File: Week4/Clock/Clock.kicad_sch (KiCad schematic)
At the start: 46 parts, among them J1 Power_inlet_vertical, J2 Conn_01x06, SW1 RotaryEncoder_Switch, SW2 Omron_B3F_SPST, U2 ATmega328-PU, U3 L7805_TO92, U4 DS1307_DIP-8, U5 MAX7219, U6 MAX7219, Y1 Crystal 16MHZ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

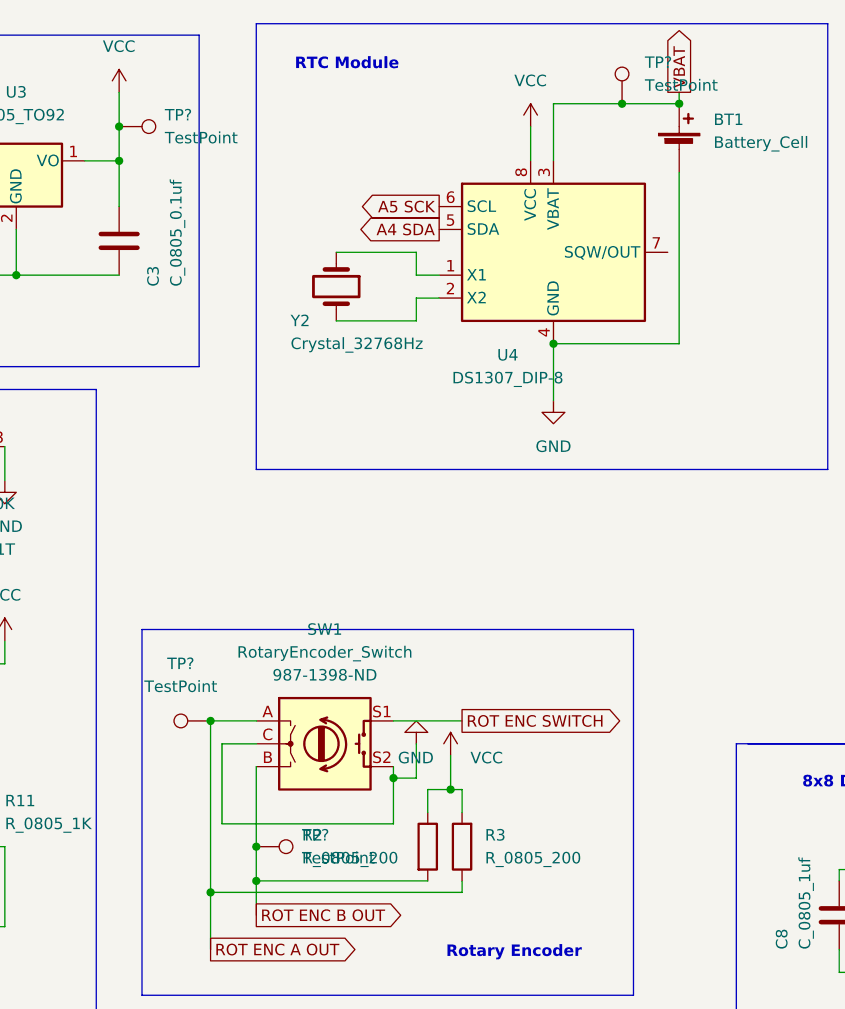
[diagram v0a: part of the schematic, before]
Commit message: Fixed ALL DRC Warnings
Mark the works of this Github Commit, this clock PCB will be amazing (Added proper logo to PCB and Schema)
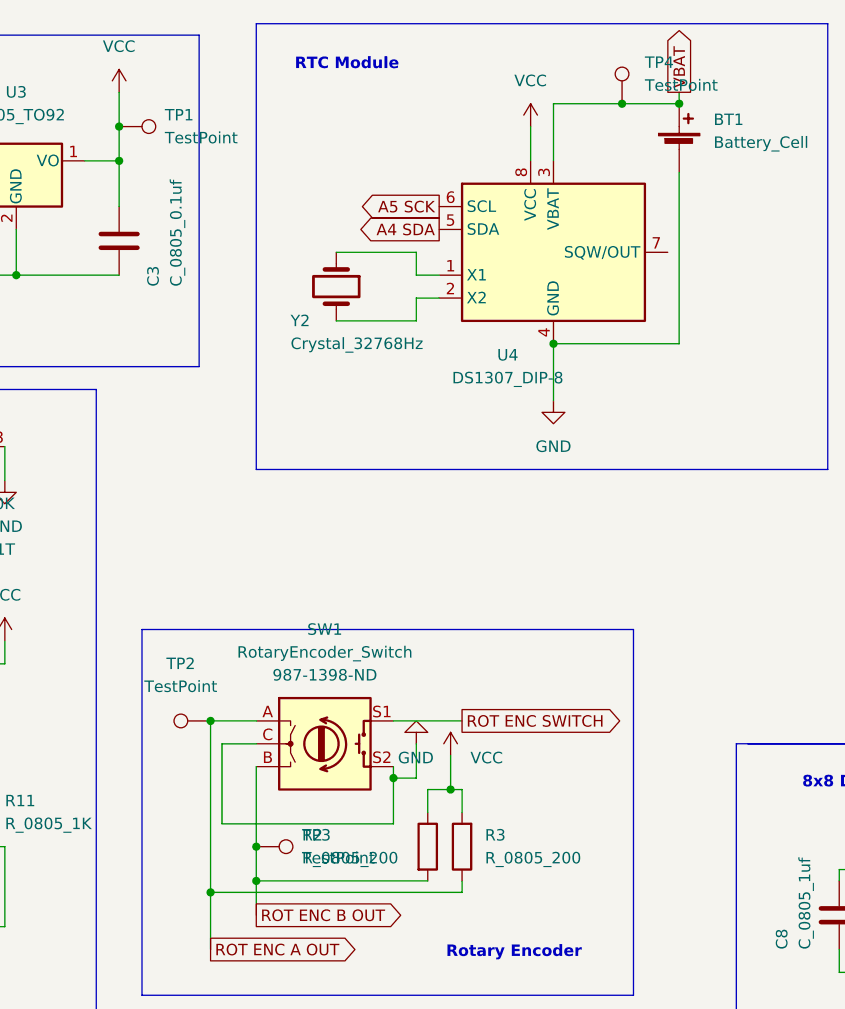
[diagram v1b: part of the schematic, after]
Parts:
- gave numbers to parts that had none: 4
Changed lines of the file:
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@@
   (symbol (lib_id "HPS:TestPoint") (at 80.01 92.71 90) (unit 1)
     (in_bom yes) (on_board yes) (fields_autoplaced)
-    (property "Reference" "TP?" (id 0) (at 76.708 86.36 90))
+    (property "Reference" "TP2" (id 0) (at 76.708 86.36 90))
     (property "Value" "TestPoint" (id 1) (at 76.708 88.9 90))
     (property "Footprint" "footprints:TestPoint_THTPad_D2.0mm_Drill1.0mm" (id 2) (at 80.01 87.63 0)
@@
   (symbol (lib_id "HPS:HPS_Logo") (at 234.95 33.02 0) (unit 1)
     (in_bom yes) (on_board yes) (fields_autoplaced)
-    (property "Reference" "#G?" (id 0) (at 234.95 26.1504 0)
+    (property "Reference" "#G1" (id 0) (at 234.95 26.1504 0)
       (effects (font (size 1.27 1.27)) hide)
     )
@@
   (symbol (lib_id "HPS:TestPoint") (at 69.85 26.67 270) (unit 1)
     (in_bom yes) (on_board yes) (fields_autoplaced)
-    (property "Reference" "TP?" (id 0) (at 74.93 25.3999 90)
+    (property "Reference" "TP1" (id 0) (at 74.93 25.3999 90)
       (effects (font (size 1.27 1.27)) (justify left))
     )
@@
   (symbol (lib_id "HPS:TestPoint") (at 85.09 106.68 270) (unit 1)
     (in_bom yes) (on_board yes) (fields_autoplaced)
-    (property "Reference" "TP?" (id 0) (at 90.17 105.4099 90)
+    (property "Reference" "TP3" (id 0) (at 90.17 105.4099 90)
       (effects (font (size 1.27 1.27)) (justify left))
     )
@@
   (symbol (lib_id "HPS:TestPoint") (at 125.73 24.13 0) (unit 1)
     (in_bom yes) (on_board yes) (fields_autoplaced)
-    (property "Reference" "TP?" (id 0) (at 128.27 19.5579 0)
+    (property "Reference" "TP4" (id 0) (at 128.27 19.5579 0)
       (effects (font (size 1.27 1.27)) (justify left))
     )
@@
   (symbol_instances
     (path "/5bb8bad9-6733-440e-9263-bd10135d64ff"
-      (reference "#G?") (unit 1) (value "HPS_Logo") (footprint "")
+      (reference "#G1") (unit 1) (value "HPS_Logo") (footprint "")
     )
     (path "/fb4d5b8c-776c-40ea-804f-0ca9c5d8e8fe"
@@
       (reference "SW2") (unit 1) (value "Omron_B3F_SPST") (footprint "footprints:SW_SPST_Omron_B3FS-100xP")
     )
+    (path "/5be55864-1840-4ba0-9935-063223afd7aa"
+      (reference "TP1") (unit 1) (value "TestPoint") (footprint "footprints:TestPoint_THTPad_D2.0mm_Drill1.0mm")
+    )
     (path "/41fa1549-a7b3-4f2a-ad55-915c96dd6f86"
-      (reference "TP?") (unit 1) (value "TestPoint") (footprint "footprints:TestPoint_THTPad_D2.0mm_Drill1.0mm")
-    )
-    (path "/5be55864-1840-4ba0-9935-063223afd7aa"
-      (reference "TP?") (unit 1) (value "TestPoint") (footprint "footprints:TestPoint_THTPad_D2.0mm_Drill1.0mm")
+      (reference "TP2") (unit 1) (value "TestPoint") (footprint "footprints:TestPoint_THTPad_D2.0mm_Drill1.0mm")
     )
     (path "/8612a2a6-32d5-4181-b693-eee795dcd550"
-      (reference "TP?") (unit 1) (value "TestPoint") (footprint "footprints:TestPoint_THTPad_D2.0mm_Drill1.0mm")
+      (reference "TP3") (unit 1) (value "TestPoint") (footprint "footprints:TestPoint_THTPad_D2.0mm_Drill1.0mm")
     )
     (path "/bce3bea4-0469-49ec-812b-abf25e966a25"
-      (reference "TP?") (unit 1) (value "TestPoint") (footprint "footprints:TestPoint_THTPad_D2.0mm_Drill1.0mm")
+      (reference "TP4") (unit 1) (value "TestPoint") (footprint "footprints:TestPoint_THTPad_D2.0mm_Drill1.0mm")
     )
     (path "/d1c2159c-cf17-43fd-99c0-c5e908f82a85"

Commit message: Added Fetus Arduino Code
Baby Clock Code has been added
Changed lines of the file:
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@@
     (pin "2")
+  )
+  (symbol (lib_id "Logo:LOGO") (at 245.11 58.42 0) (unit 1)
+    (in_bom yes) (on_board yes) (fields_autoplaced)
+    (property "Reference" "#G2" (id 0) (at 245.11 37.8175 0)
+      (effects (font (size 1.27 1.27)) hide)
+    )
+    (property "Value" "LOGO" (id 1) (at 245.11 79.0225 0)
+      (effects (font (size 1.27 1.27)) hide)
+    )
+    (property "Footprint" "" (id 2) (at 245.11 58.42 0)
+      (effects (font (size 1.27 1.27)) hide)
+    )
+    (property "Datasheet" "" (id 3) (at 245.11 58.42 0)
+      (effects (font (size 1.27 1.27)) hide)
+    )
   )
   (symbol (lib_id "HPS:VCC") (at 57.15 83.82 0) (unit 1)
@@
       (reference "#G1") (unit 1) (value "HPS_Logo") (footprint "")
     )
+    (path "/f46ac623-4ddf-4dd9-909e-dde17c33c099"
+      (reference "#G2") (unit 1) (value "LOGO") (footprint "")
+    )
     (path "/fb4d5b8c-776c-40ea-804f-0ca9c5d8e8fe"

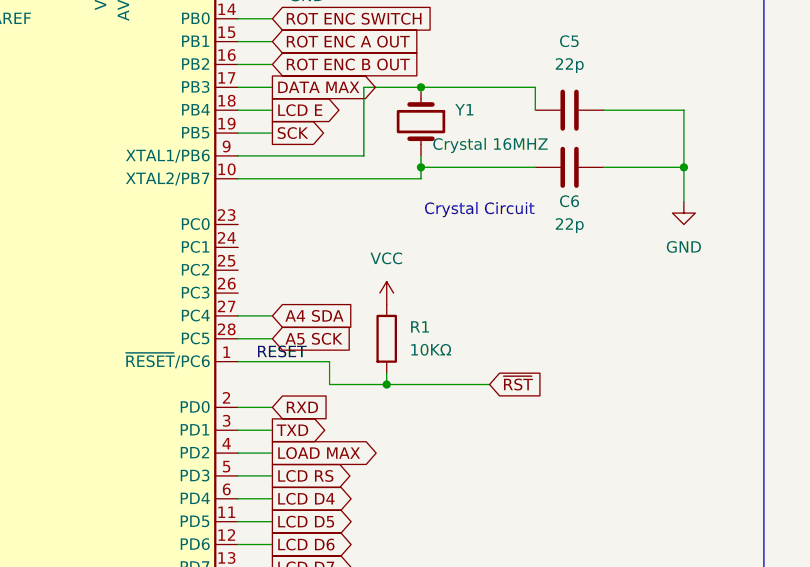
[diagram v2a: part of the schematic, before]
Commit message: Week 6 Update* (Arduino Code)
Added additional Display modes now including Decimal and Binary mode found at https://bryang229.github.io/8x8Demo/ :) now we have 3 different ways to read time !
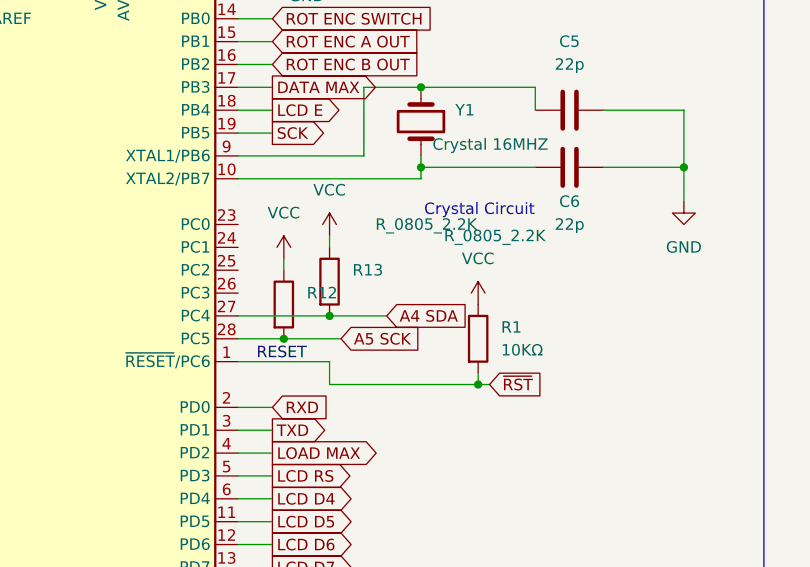
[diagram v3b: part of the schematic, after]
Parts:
- added R12, R13: R_0805_2.2K, footprints:R_0805_2012Metric, symbol HPS:R_0805_2.2K
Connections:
- net A4 SDA: now also R13.2
- net A5 SCK: now also R12.2
- net VCC: now also R12.1, R13.1
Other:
- moved on the sheet: R1
